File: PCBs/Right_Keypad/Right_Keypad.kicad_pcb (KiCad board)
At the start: 2 copper layers, 73.7 x 91.4 mm, 33 parts, among them J1 Conn_Right_Keypad, SW1 SW_Push, SW10 SW_Push, SW11 SW_Push, SW12 SW_Push, SW13 SW_Push, SW14 SW_Push, SW15 SW_Push, SW16 SW_Push, SW17 SW_Push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

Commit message: before moving keypad shift regs
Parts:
- added REF**: MountingHole, MountingHole:MountingHole_3.2mm_M3, F.Cu at (96.5, 144.1)
- added REF**: MountingHole_3.2mm_M3, MountingHole:MountingHole_3.2mm_M3, F.Cu at (174.0, 49.5)
- added REF**: MountingHole_3.2mm_M3, MountingHole:MountingHole_3.2mm_M3, F.Cu at (174.0, 144.1)
- added REF**: MountingHole_3.2mm_M3, MountingHole:MountingHole_3.2mm_M3, F.Cu at (96.5, 49.5)
- moved R1 58.4 mm to (121.9, 140.3), turned to 180 degrees
- moved C1 24.1 mm to (116.9, 116.2)
- moved C2 24.1 mm to (130.8, 116.2)
- moved C3 24.1 mm to (102.9, 116.2)
- moved RN1 22.9 mm to (111.1, 116.8), turned to -90 degrees
- moved RN2 22.9 mm to (125.1, 116.8), turned to -90 degrees
- moved RN3 22.9 mm to (139.1, 116.8), turned to -90 degrees
- moved J1 9.94 mm to (130.8, 102.2), turned to -90 degrees
- moved SW10 1.27 mm to (104.1, 113.0)
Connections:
- SW1 pad 2: Net-(RN1-R8) -> Net-(RN1-R4)
- SW10 pad 2: Net-(RN2-R7) -> Net-(RN1-R1)
- SW11 pad 2: Net-(RN2-R6) -> Net-(RN2-R3)
- SW12 pad 2: Net-(RN2-R5) -> Net-(RN2-R4)
- SW13 pad 2: Net-(RN2-R4) -> Net-(RN2-R5)
- SW14 pad 2: Net-(RN2-R3) -> Net-(RN3-R3)
- SW15 pad 2: Net-(RN2-R2) -> Net-(RN3-R4)
- SW16 pad 2: Net-(RN2-R1) -> Net-(RN3-R5)
- SW17 pad 2: Net-(RN3-R8) -> Net-(RN2-R6)
- SW18 pad 2: Net-(RN3-R7) -> Net-(RN2-R7)
- SW19 pad 2: Net-(RN3-R6) -> Net-(RN2-R8)
- SW2 pad 2: Net-(RN1-R7) -> Net-(RN1-R5)
- SW20 pad 2: Net-(RN3-R5) -> Net-(RN3-R6)
- SW21 pad 2: Net-(RN3-R4) -> Net-(RN3-R7)
- SW22 pad 2: Net-(RN3-R3) -> Net-(RN3-R8)
- SW3 pad 2: Net-(RN1-R6) -> Net-(RN1-R8)
- SW4 pad 2: Net-(RN1-R5) -> Net-(RN1-R3)
- SW5 pad 2: Net-(RN1-R4) -> Net-(RN1-R6)
- SW6 pad 2: Net-(RN1-R3) -> Net-(RN2-R2)
- SW8 pad 2: Net-(RN1-R1) -> Net-(RN1-R7)
- SW9 pad 2: Net-(RN2-R8) -> Net-(RN2-R1)
- U1 pad 12: Net-(RN1-R7) -> Net-(RN1-R6)
- U1 pad 13: Net-(RN1-R6) -> Net-(RN1-R4)
- U1 pad 14: Net-(RN1-R5) -> Net-(RN1-R2)
- U1 pad 3: Net-(RN1-R4) -> Net-(RN1-R1)
- U1 pad 5: Net-(RN1-R2) -> Net-(RN1-R5)
- U1 pad 6: Net-(RN1-R1) -> Net-(RN1-R7)
- U2 pad 12: Net-(RN2-R7) -> Net-(RN2-R6)
- U2 pad 13: Net-(RN2-R6) -> Net-(RN2-R4)
- U2 pad 14: Net-(RN2-R5) -> Net-(RN2-R2)
- U2 pad 3: Net-(RN2-R4) -> Net-(RN2-R1)
- U2 pad 5: Net-(RN2-R2) -> Net-(RN2-R5)
- U2 pad 6: Net-(RN2-R1) -> Net-(RN2-R7)
- U3 pad 12: Net-(RN3-R7) -> Net-(RN3-R6)
- U3 pad 13: Net-(RN3-R6) -> Net-(RN3-R4)
- U3 pad 14: Net-(RN3-R5) -> Net-(RN3-R2)
- U3 pad 3: Net-(RN3-R4) -> Net-(RN3-R1)
- U3 pad 5: Net-(RN3-R2) -> Net-(RN3-R5)
- U3 pad 6: Net-(RN3-R1) -> Net-(RN3-R7)
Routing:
- net Net-(RN1-R8): track 0.00 -> 114.1 mm
- net Net-(RN1-R5): track 0.00 -> 107.6 mm
- net Net-(RN3-R3): track 0.00 -> 105.4 mm
- net Net-(RN2-R3): track 0.00 -> 95.5 mm
- net Net-(RN1-R6): track 0.00 -> 87.2 mm
- net Net-(RN3-R4): track 0.00 -> 83.2 mm
- net Net-(RN1-R4): track 0.00 -> 82.0 mm
- net Net-(RN3-R5): track 0.00 -> 78.7 mm
- net Net-(RN2-R4): track 0.00 -> 77.3 mm
- net Net-(RN2-R5): track 0.00 -> 75.3 mm
- net Net-(RN1-R3): track 0.00 -> 70.2 mm
- net Net-(RN1-R7): track 0.00 -> 69.3 mm
- net Net-(RN2-R2): track 0.00 -> 63.5 mm
- net Net-(RN2-R7): track 0.00 -> 56.7 mm
- net Net-(RN3-R6): track 0.00 -> 56.7 mm
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- added copper zone on In2.Cu, net +5V
- added copper zone on In1.Cu, net GND
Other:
- board size 73.7 x 91.4 mm -> 86.4 x 103.6 mm
- copper layers 2 -> 4
- board text added: "3.2mm_M3"

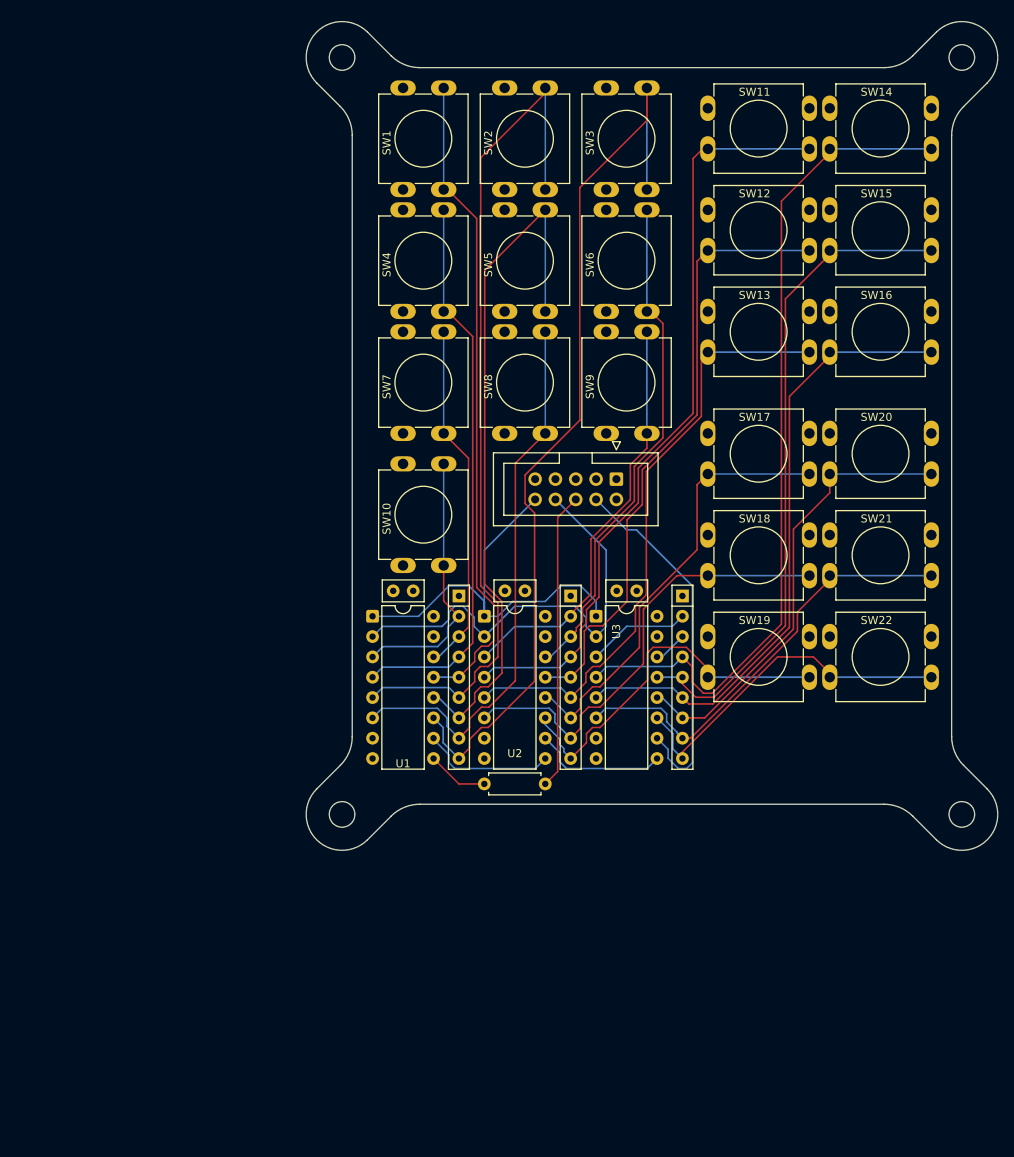
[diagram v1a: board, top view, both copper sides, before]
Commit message: Moved shift registers
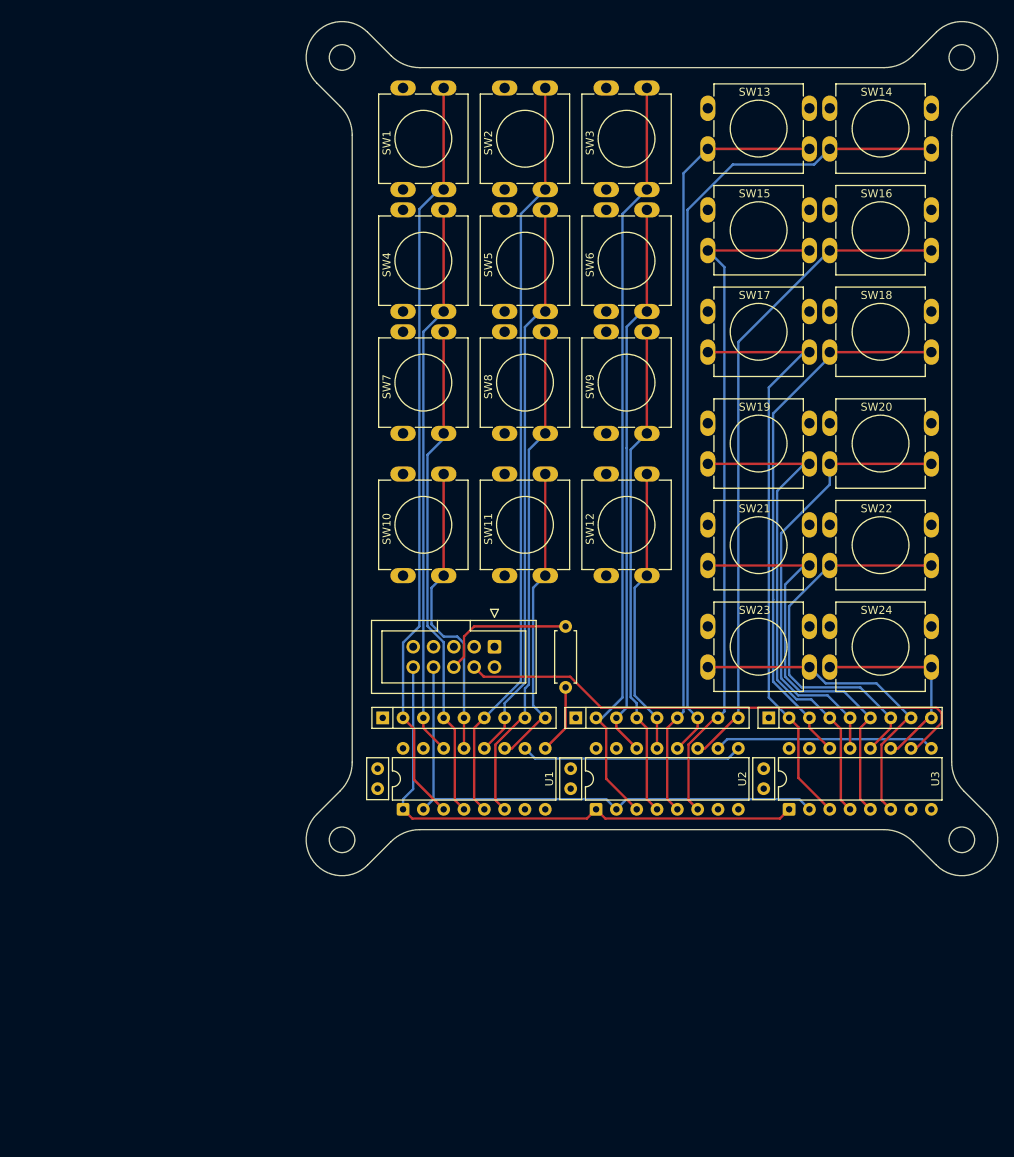
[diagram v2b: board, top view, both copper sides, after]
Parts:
- added SW23: SW_Push, Custom_Footprints:SW_PUSH-12mm_Grid, F.Cu at (142.2, 120.7)
- added SW24: SW_Push, Custom_Footprints:SW_PUSH-12mm_Grid, F.Cu at (157.5, 120.7)
- REF**: value MountingHole -> MountingHole_3.2mm_M3
- moved SW11 63.7 mm to (116.8, 114.3), turned to 90 degrees
- moved SW12 47.5 mm to (129.5, 114.3), turned to 90 degrees
- moved U3 34.1 mm to (152.4, 143.5), turned to 90 degrees
- moved SW18 31.8 mm to (157.5, 81.3)
- moved C2 30.8 mm to (149.2, 140.9), turned to 90 degrees
- moved U2 27.9 mm to (128.3, 143.5), turned to 90 degrees
- moved SW19 26.7 mm to (142.2, 95.2)
- moved C1 26.1 mm to (125.1, 140.9), turned to 90 degrees
- moved J1 25.9 mm to (115.6, 123.2)
- moved SW13 25.4 mm to (142.2, 55.9)
- moved C3 24.8 mm to (101.0, 140.9), turned to 90 degrees
- moved U1 24.4 mm to (104.1, 143.5), turned to 90 degrees
- moved R1 19.8 mm to (124.5, 120.7), turned to -90 degrees
- moved RN3 18.7 mm to (149.9, 132.1), turned to 0 degrees
- moved RN1 18.0 mm to (101.6, 132.1), turned to 0 degrees
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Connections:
- SW1 pad 2: Net-(RN1-R4) -> Net-(RN1-R1)
- SW10 pad 2: Net-(RN1-R1) -> Net-(RN1-R4)
- SW11 pad 2: Net-(RN2-R3) -> Net-(RN1-R8)
- SW14 pad 2: Net-(RN3-R3) -> Net-(RN2-R6)
- SW15 pad 2: Net-(RN3-R4) -> Net-(RN2-R7)
- SW16 pad 2: Net-(RN3-R5) -> Net-(RN2-R8)
- SW17 pad 2: Net-(RN2-R6) -> Net-(RN3-R1)
- SW18 pad 2: Net-(RN2-R7) -> Net-(RN3-R2)
- SW19 pad 2: Net-(RN2-R8) -> Net-(RN3-R3)
- SW20 pad 2: Net-(RN3-R6) -> Net-(RN3-R4)
- SW21 pad 2: Net-(RN3-R7) -> Net-(RN3-R5)
- SW22 pad 2: Net-(RN3-R8) -> Net-(RN3-R6)
- SW3 pad 2: Net-(RN1-R8) -> Net-(RN2-R1)
- SW4 pad 2: Net-(RN1-R3) -> Net-(RN1-R2)
- SW7 pad 2: Net-(RN1-R2) -> Net-(RN1-R3)
- SW9 pad 2: Net-(RN2-R1) -> Net-(RN2-R3)
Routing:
- net Net-(RN1-R8): track 114.1 -> 38.4 mm
- net Net-(RN3-R2): track 4.23 -> 68.1 mm
- net Net-(RN3-R1): track 12.9 -> 75.5 mm
- net Net-(RN1-R1): track 33.4 -> 94.7 mm
- net Net-(RN2-R6): track 55.1 -> 102.5 mm
- net Net-(RN1-R4): track 82.0 -> 37.6 mm
- net Net-(RN2-R1): track 52.4 -> 95.4 mm
- net Net-(RN3-R3): track 105.4 -> 62.8 mm
- net Net-(RN2-R4): track 77.3 -> 36.1 mm
- net Net-(RN2-R8): track 46.8 -> 82.5 mm
- net Net-(RN2-R3): track 95.5 -> 61.9 mm
- net Net-(RN2-R7): track 56.7 -> 86.0 mm
- net Net-(RN3-R4): track 83.2 -> 56.5 mm
- net Net-(RN1-R2): track 44.1 -> 69.4 mm
- net Net-(RN3-R5): track 78.7 -> 53.5 mm
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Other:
- board size 86.4 x 103.6 mm -> 86.4 x 106.8 mm
- board text removed: "3.2mm_M3"

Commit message: wip
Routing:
- net Net-(RN1-R8): track 38.4 -> 40.5 mm
- net Net-(RN1-R7): track 63.0 -> 64.6 mm
- net Net-(J1-IN_DFM): track 67.2 -> 68.0 mm
- net Net-(J1-IN_DTM): vias 0 -> 1
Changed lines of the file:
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@@
 			(outputformat 1)
 			(mirror no)
-			(drillshape 1)
+			(drillshape 0)
 			(scaleselection 1)
-			(outputdirectory "")
+			(outputdirectory "fab/gerber/drill")
 		)
 	)
@@
 	(segment
 		(start 113.03 120.65)
-		(end 111.76 121.92)
+		(end 116.586 120.65)
 		(width 0.3)
 		(layer "F.Cu")
@@
 	)
 	(segment
-		(start 111.76 121.92)
-		(end 111.76 124.46)
+		(start 116.586 120.65)
+		(end 118.872 120.65)
 		(width 0.3)
 		(layer "F.Cu")
@@
 	)
 	(segment
-		(start 124.46 120.65)
-		(end 113.03 120.65)
+		(start 111.76 121.92)
+		(end 111.76 124.46)
 		(width 0.3)
 		(layer "F.Cu")
@@
 	)
 	(segment
-		(start 114.231 126.931)
-		(end 125.026 126.931)
-		(width 0.3)
-		(layer "F.Cu")
-		(net 6)
-	)
-	(segment
-		(start 170.815 130.81)
-		(end 171.45 131.445)
+		(start 111.76 121.92)
+		(end 113.03 120.65)
 		(width 0.3)
 		(layer "F.Cu")
-		(net 6)
+		(net 5)
 	)
-	(segment
-		(start 128.905 130.81)
-		(end 170.815 130.81)
-		(width 0.3)
-		(layer "F.Cu")
-		(net 6)
+	(via
+		(at 118.872 120.65)
+		(size 0.6)
+		(drill 0.3)
+		(layers "F.Cu" "B.Cu")
+		(net 5)
 	)
 	(segment
-		(start 171.45 131.445)
-		(end 171.45 132.715)
+		(start 118.872 120.65)
+		(end 124.46 120.65)
 		(width 0.3)
-		(layer "F.Cu")
-		(net 6)
+		(layer "B.Cu")
+		(net 5)
 	)
 	(segment
-		(start 171.45 132.715)
-		(end 168.275 135.89)
+		(start 113.03 136.24776)
+		(end 113.03 125.73)
 		(width 0.3)
-		(layer "F.Cu")
+		(layer "B.Cu")
 		(net 6)
 	)
 	(segment
-		(start 125.026 126.931)
-		(end 128.905 130.81)
+		(start 167.64 135.89)
+		(end 163.949 139.581)
 		(width 0.3)
-		(layer "F.Cu")
+		(layer "B.Cu")
 		(net 6)
 	)
 	(segment
-		(start 168.275 135.89)
-		(end 167.64 135.89)
+		(start 163.949 139.581)
+		(end 116.36324 139.581)
 		(width 0.3)
-		(layer "F.Cu")
+		(layer "B.Cu")
 		(net 6)
 	)
 	(segment
-		(start 113.03 125.73)
-		(end 114.231 126.931)
+		(start 116.36324 139.581)
+		(end 113.03 136.24776)
 		(width 0.3)
-		(layer "F.Cu")
+		(layer "B.Cu")
 		(net 6)
 	)
@@
 		(end 124.46 133.35)
 		(width 0.3)
-		(layer "F.Cu")
+		(layer "B.Cu")
 		(net 7)
 	)
@@
 		(end 121.92 135.89)
 		(width 0.3)
-		(layer "F.Cu")
+		(layer "B.Cu")
 		(net 7)
 	)
@@
 	(segment
 		(start 114.3 132.08)
-		(end 118.872 127.508)
+		(end 114.3 73.66)
 		(width 0.3)
 		(layer "B.Cu")
@@
 	)
 	(segment
-		(start 118.872 69.088)
+		(start 114.3 73.66)
 		(end 121.92 66.04)
 		(width 0.3)
@@
 	)
 	(segment
-		(start 118.872 127.508)
-		(end 118.872 69.088)
-		(width 0.3)
-		(layer "B.Cu")
-		(net 8)
-	)
-	(segment
 		(start 109.22 132.08)
 		(end 110.609 133.469)
@@
 	)
 	(segment
-		(start 116.84 132.08)
-		(end 116.84 130.247106)
+		(start 116.84 117.965788)
+		(end 119.372 115.433788)
 		(width 0.3)
 		(layer "B.Cu")
@@
 	)
 	(segment
-		(start 119.372 83.228)
-		(end 121.32 81.28)
+		(start 116.84 132.08)
+		(end 116.84 117.965788)
 		(width 0.3)
 		(layer "B.Cu")
@@
 	)
 	(segment
-		(start 119.372 127.715106)
-		(end 119.372 83.228)
+		(start 121.32 81.28)
+		(end 121.92 81.28)
 		(width 0.3)
 		(layer "B.Cu")
@@
 	)
 	(segment
-		(start 116.84 130.247106)
-		(end 119.372 127.715106)
+		(start 119.372 115.433788)
+		(end 119.372 83.228)
 		(width 0.3)
 		(layer "B.Cu")
@@
 	)
 	(segment
-		(start 121.32 81.28)
-		(end 121.92 81.28)
+		(start 119.372 83.228)
+		(end 121.32 81.28)
 		(width 0.3)
 		(layer "B.Cu")
@@
 	)
 	(segment
-		(start 119.38 128.414212)
-		(end 119.872 127.922212)
+		(start 119.872 115.640894)
+		(end 119.872 98.568)
 		(width 0.3)
 		(layer "B.Cu")
@@
 	(segment
 		(start 119.38 132.08)
-		(end 119.38 128.414212)
+		(end 117.356 130.056)
 		(width 0.3)
 		(layer "B.Cu")
@@
 	)
 	(segment
-		(start 119.872 127.922212)
-		(end 119.872 98.568)
+		(start 117.356 118.156894)
+		(end 119.872 115.640894)
+		(width 0.3)
+		(layer "B.Cu")
+		(net 12)
+	)
+	(segment
+		(start 117.356 130.056)
+		(end 117.356 118.156894)
 		(width 0.3)
 		(layer "B.Cu")
@@
 	)
 	(segment
-		(start 120.396 115.824)
-		(end 121.92 114.3)
+		(start 121.92 132.08)
+		(end 117.856 128.016)
 		(width 0.3)
 		(layer "B.Cu")
@@
 	)
 	(segment
-		(start 121.92 132.08)
-		(end 120.396 130.556)
+		(start 117.856 128.016)
+		(end 117.856 118.364)
 		(width 0.3)
 		(layer "B.Cu")
@@
 	)
 	(segment
-		(start 120.396 130.556)
-		(end 120.396 115.824)
+		(start 117.856 118.364)
+		(end 121.92 114.3)
 		(width 0.3)
 		(layer "B.Cu")

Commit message: before UART+RS485
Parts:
- removed C2, C3: 100nF, Capacitor_THT:C_Disc_D5.0mm_W2.5mm_P2.50mm
- removed REF** (x4): MountingHole_3.2mm_M3, MountingHole:MountingHole_3.2mm_M3
- removed RN2, RN3: R_Network08, Resistor_THT:R_Array_SIP9
- removed U2, U3: 74HC165, Package_DIP:DIP-16_W7.62mm
- added D1: D, Diode_SMD:D_SOD-123, B.Cu at (106.7, 59.7)
- added D10: D, Diode_SMD:D_SOD-123, B.Cu at (106.7, 108.0)
- added D11: D, Diode_SMD:D_SOD-123, B.Cu at (119.4, 108.0)
- added D12: D, Diode_SMD:D_SOD-123, B.Cu at (132.1, 108.0)
- added D13: D, Diode_SMD:D_SOD-123, B.Cu at (148.6, 58.4)
- added D14: D, Diode_SMD:D_SOD-123, B.Cu at (163.8, 58.4)
- added D15: D, Diode_SMD:D_SOD-123, B.Cu at (148.6, 71.1)
- added D16: D, Diode_SMD:D_SOD-123, B.Cu at (163.8, 71.1)
- added D17: D, Diode_SMD:D_SOD-123, B.Cu at (148.6, 83.8)
- added D18: D, Diode_SMD:D_SOD-123, B.Cu at (163.8, 83.8)
- added D19: D, Diode_SMD:D_SOD-123, B.Cu at (148.6, 97.8)
- added D2: D, Diode_SMD:D_SOD-123, B.Cu at (119.4, 59.7)
- added D20: D, Diode_SMD:D_SOD-123, B.Cu at (163.8, 97.8)
- added D21: D, Diode_SMD:D_SOD-123, B.Cu at (148.6, 110.5)
- added D22: D, Diode_SMD:D_SOD-123, B.Cu at (163.8, 110.5)
- added D23: D, Diode_SMD:D_SOD-123, B.Cu at (148.6, 123.2)
- added D24: D, Diode_SMD:D_SOD-123, B.Cu at (163.8, 123.2)
- added D3: D, Diode_SMD:D_SOD-123, B.Cu at (132.1, 59.7)
- added D4: D, Diode_SMD:D_SOD-123, B.Cu at (106.7, 74.9)
- added D5: D, Diode_SMD:D_SOD-123, B.Cu at (119.4, 74.9)
- added D6: D, Diode_SMD:D_SOD-123, B.Cu at (132.1, 74.9)
- added D7: D, Diode_SMD:D_SOD-123, B.Cu at (106.7, 90.2)
- added D8: D, Diode_SMD:D_SOD-123, B.Cu at (119.4, 90.2)
- added D9: D, Diode_SMD:D_SOD-123, B.Cu at (132.1, 90.2)
- added Q1: NPN, Package_TO_SOT_THT:TO-92_Inline, F.Cu at (57.1, 158.8)
- added Q2: NPN, Package_TO_SOT_THT:TO-92_Inline, F.Cu at (57.1, 164.5)
- added Q3: NPN, Package_TO_SOT_THT:TO-92_Inline, F.Cu at (57.1, 170.3)
- added R2: 10k, Resistor_THT:R_Axial_DIN0207_L6.3mm_D2.5mm_P7.62mm_Horizontal, B.Cu at (168.9, 184.2)
- added R3: 10k, Resistor_THT:R_Axial_DIN0207_L6.3mm_D2.5mm_P7.62mm_Horizontal, B.Cu at (143.5, 184.2)
- added R4: 10k, Resistor_THT:R_Axial_DIN0207_L6.3mm_D2.5mm_P7.62mm_Horizontal, B.Cu at (118.1, 184.2)
- J1: footprint Connector_IDC:IDC-Header_2x05_P2.54mm_Vertical -> Connector_IDC:IDC-Header_2x08_P2.54mm_Vertical
- moved R1 34.7 mm to (141.0, 151.1)
- moved J1 34.1 mm to (146.1, 138.4), turned to 90 degrees
- moved U1 20.5 mm to (106.7, 123.2), turned to 0 degrees
- moved RN1 20.1 mm to (118.1, 143.5), turned to 90 degrees
- moved C1 16.2 mm to (109.3, 144.1), turned to 0 degrees
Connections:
- RN1 pad 2: Net-(RN1-R1) -> Net-(D16-A)
- RN1 pad 3: Net-(RN1-R2) -> Net-(D15-A)
- RN1 pad 4: Net-(RN1-R3) -> Net-(D14-A)
- RN1 pad 5: Net-(RN1-R4) -> Net-(D13-A)
- RN1 pad 6: Net-(RN1-R5) -> Net-(D12-A)
- RN1 pad 7: Net-(RN1-R6) -> Net-(D11-A)
- RN1 pad 8: Net-(RN1-R7) -> Net-(D10-A)
- RN1 pad 9: Net-(RN1-R8) -> Net-(D1-A)
- SW1 pad 1: GND -> Net-(Q1-C)
- SW1 pad 2: Net-(RN1-R1) -> Net-(D1-K)
- SW10 pad 1: GND -> Net-(Q2-C)
- SW10 pad 2: Net-(RN1-R4) -> Net-(D10-K)
- SW11 pad 1: GND -> Net-(Q2-C)
- SW11 pad 2: Net-(RN1-R8) -> Net-(D11-K)
- SW12 pad 1: GND -> Net-(Q2-C)
- SW13 pad 1: GND -> Net-(Q2-C)
- SW14 pad 1: GND -> Net-(Q2-C)
- SW15 pad 1: GND -> Net-(Q2-C)
- SW16 pad 1: GND -> Net-(Q2-C)
- SW17 pad 1: GND -> Net-(Q3-C)
- SW18 pad 1: GND -> Net-(Q3-C)
- SW19 pad 1: GND -> Net-(Q3-C)
- SW2 pad 1: GND -> Net-(Q1-C)
- SW2 pad 2: Net-(RN1-R5) -> Net-(D2-K)
- SW20 pad 1: GND -> Net-(Q3-C)
- SW21 pad 1: GND -> Net-(Q3-C)
- SW22 pad 1: GND -> Net-(Q3-C)
- SW23 pad 1: GND -> Net-(Q3-C)
- SW24 pad 1: GND -> Net-(Q3-C)
- SW3 pad 1: GND -> Net-(Q1-C)
- SW4 pad 1: GND -> Net-(Q1-C)
- SW4 pad 2: Net-(RN1-R2) -> Net-(D4-K)
- SW5 pad 1: GND -> Net-(Q1-C)
- SW5 pad 2: Net-(RN1-R6) -> Net-(D5-K)
- SW6 pad 1: GND -> Net-(Q1-C)
- SW7 pad 1: GND -> Net-(Q1-C)
- SW7 pad 2: Net-(RN1-R3) -> Net-(D7-K)
- SW8 pad 1: GND -> Net-(Q1-C)
- SW8 pad 2: Net-(RN1-R7) -> Net-(D8-K)
- SW9 pad 1: GND -> Net-(Q2-C)
- U1 pad 10: Net-(U1-DS) -> Net-(J1-IN_DFM)
- U1 pad 11: Net-(RN1-R8) -> Net-(D1-A)
- U1 pad 12: Net-(RN1-R6) -> Net-(D10-A)
- U1 pad 13: Net-(RN1-R4) -> Net-(D11-A)
- U1 pad 14: Net-(RN1-R2) -> Net-(D12-A)
- U1 pad 3: Net-(RN1-R1) -> Net-(D13-A)
- U1 pad 4: Net-(RN1-R3) -> Net-(D14-A)
- U1 pad 5: Net-(RN1-R5) -> Net-(D15-A)
- U1 pad 6: Net-(RN1-R7) -> Net-(D16-A)
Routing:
- net Net-(Q2-C): track 0.00 -> 192.8 mm
- net Net-(Q3-C): track 0.00 -> 154.4 mm
- net Net-(Q1-C): track 0.00 -> 141.9 mm
- net Net-(RN1-R1): track 94.7 -> 0.00 mm
- net Net-(RN1-R5): track 94.4 -> 0.00 mm
- net Net-(D14-K): track 102.5 -> 19.4 mm
- net Net-(D13-K): track 97.9 -> 19.4 mm
- net Net-(D3-K): track 95.4 -> 19.4 mm
- net Net-(RN1-R6): track 70.8 -> 0.00 mm
- net Net-(RN1-R2): track 69.4 -> 0.00 mm
- net Net-(J1-IN_PL): track 68.5 -> 0.00 mm
- net Net-(J1-IN_DFM): track 68.0 -> 0.00 mm
- net Net-(J1-IN_CP): track 66.9 -> 0.00 mm
- net Net-(D15-K): track 86.0 -> 19.4 mm
- net Net-(RN1-R7): track 64.6 -> 0.00 mm
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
